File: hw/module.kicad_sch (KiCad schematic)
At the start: 42 parts, among them Q1 MUN 2211, U1 CFPS-39, U2 CFPS-39, U3 74LVC1G125, U4 74 LVC 1G3157GW,125, U5 MAX919, U6 STM32L010F4P6, U7 BAS70-7-F, U8 SS39ET

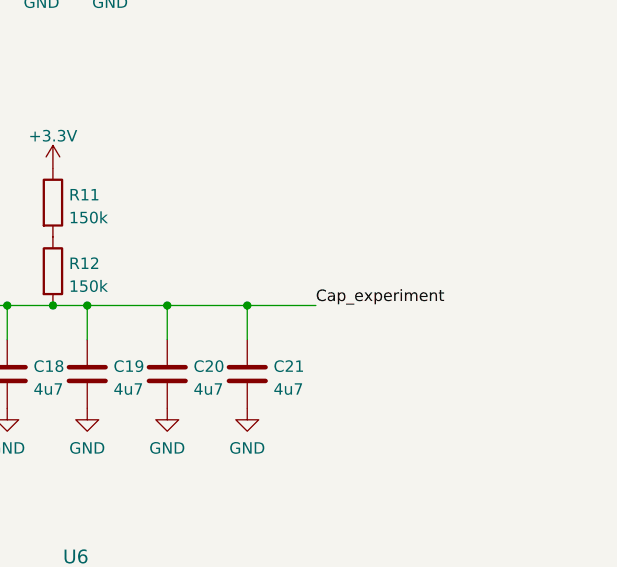
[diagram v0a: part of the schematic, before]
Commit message: Add extra resistor for capacitor measure, remove out-the-board wires
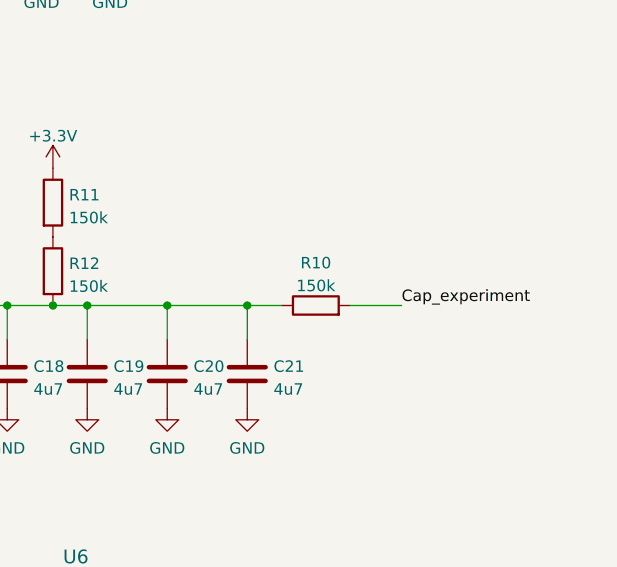
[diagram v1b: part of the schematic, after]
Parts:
- added R10: 150k, Resistor_SMD:R_0201_0603Metric_Pad0.64x0.40mm_HandSolder, symbol Device:R
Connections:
- net Cap_experiment: now also R10.2; no longer C16.1, C17.1, C18.1, C19.1, C20.1, C21.1, R12.2
- new net: C16.1, C17.1, C18.1, C19.1, C20.1, C21.1, R10.1, R12.2
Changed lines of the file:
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@@
   (junction (at 237.49 78.74) (diameter 0) (color 0 0 0 0)
   )
+  (junction (at 246.38 78.74) (diameter 0) (color 0 0 0 0)
+  )
   (junction (at 74.93 49.53) (diameter 0) (color 0 0 0 0)
   )
@@
   )
   (junction (at 228.6 78.74) (diameter 0) (color 0 0 0 0)
-  )
-  (junction (at 246.38 78.74) (diameter 0) (color 0 0 0 0)
   )
   (junction (at 231.14 33.02) (diameter 0) (color 0 0 0 0)
@@
     (stroke (width 0) (type default) (color 0 0 0 0))
   )
-  (wire (pts (xy 254 78.74) (xy 246.38 78.74))
-    (stroke (width 0) (type default) (color 0 0 0 0))
-  )
   (wire (pts (xy 257.81 138.43) (xy 281.94 138.43))
     (stroke (width 0) (type default) (color 0 0 0 0))
   )
+  (wire (pts (xy 257.81 78.74) (xy 263.525 78.74))
+    (stroke (width 0) (type default) (color 0 0 0 0))
+  )
   (wire (pts (xy 182.88 27.94) (xy 182.88 25.4))
     (stroke (width 0) (type default) (color 0 0 0 0))
@@
   )
   (wire (pts (xy 31.75 187.96) (xy 31.75 189.23))
+    (stroke (width 0) (type default) (color 0 0 0 0))
+  )
+  (wire (pts (xy 250.19 78.74) (xy 246.38 78.74))
     (stroke (width 0) (type default) (color 0 0 0 0))
   )
@@
     (effects (font (size 1.27 1.27)) (justify left bottom))
   )
-  (label "Cap_experiment" (at 254 78.74 0)
+  (label "Cap_experiment" (at 263.525 78.74 0)
     (effects (font (size 1.27 1.27)) (justify left bottom))
   )
@@
     )
     (pin "1")
+  )
+  (symbol (lib_id "Device:R") (at 254 78.74 90) (unit 1)
+    (in_bom yes) (on_board yes) (fields_autoplaced)
+    (property "Reference" "R10" (id 0) (at 254 74.0242 90))
+    (property "Value" "150k" (id 1) (at 254 76.5611 90))
+    (property "Footprint" "Resistor_SMD:R_0201_0603Metric_Pad0.64x0.40mm_HandSolder" (id 2) (at 254 80.518 90)
+      (effects (font (size 1.27 1.27)) hide)
+    )
+    (property "Datasheet" "~" (id 3) (at 254 78.74 0)
+      (effects (font (size 1.27 1.27)) hide)
+    )
+    (pin "1")
+    (pin "2")
   )
   (symbol (lib_id "power:GND") (at 31.75 189.23 0) (unit 1)
@@
       (reference "R9") (unit 1) (value "10k") (footprint "Resistor_SMD:R_0201_0603Metric_Pad0.64x0.40mm_HandSolder")
     )
+    (path "/1bc4374f-5e0f-4c16-9e5b-a3a33541057e"
+      (reference "R10") (unit 1) (value "150k") (footprint "Resistor_SMD:R_0201_0603Metric_Pad0.64x0.40mm_HandSolder")
+    )
     (path "/c3b088e6-8fb8-4f54-b8cc-ac4fee9ad1e4"

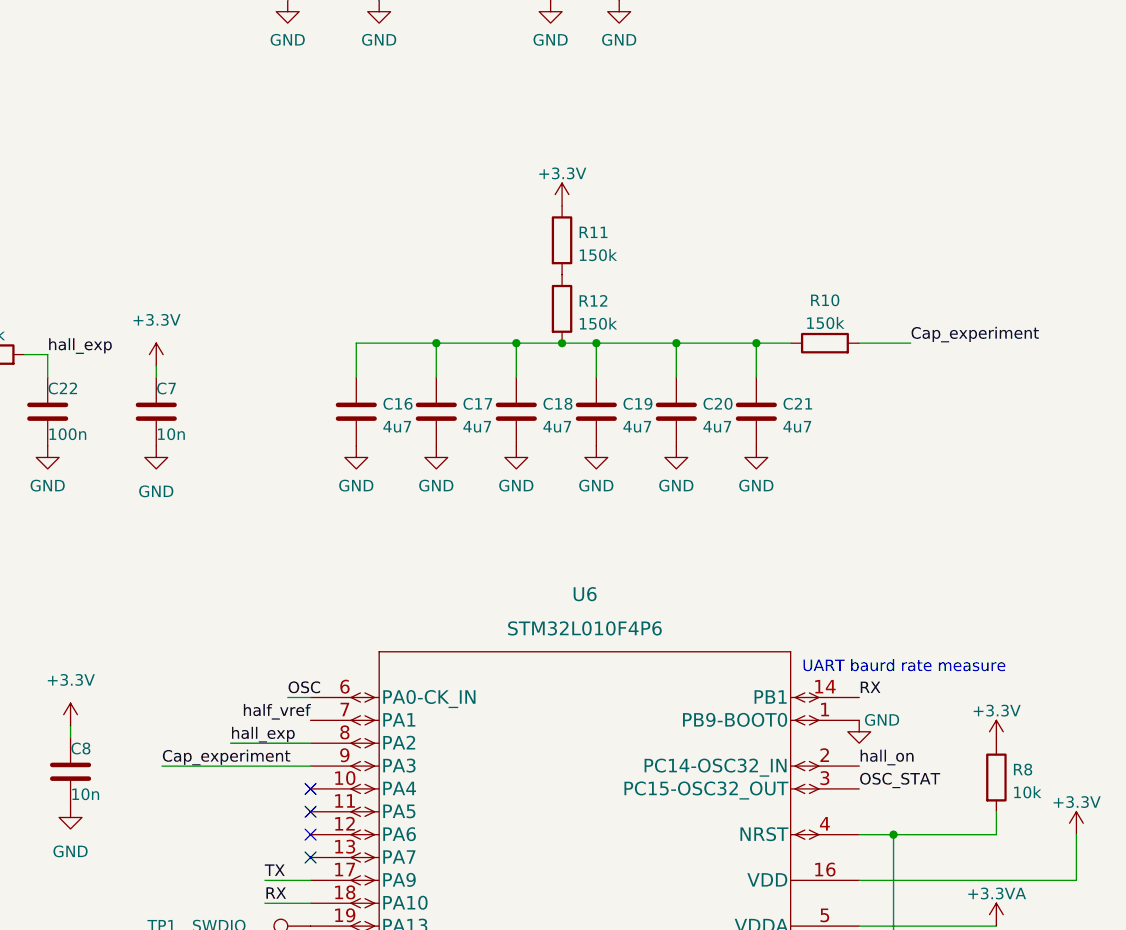
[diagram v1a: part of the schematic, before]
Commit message: 0603 passives
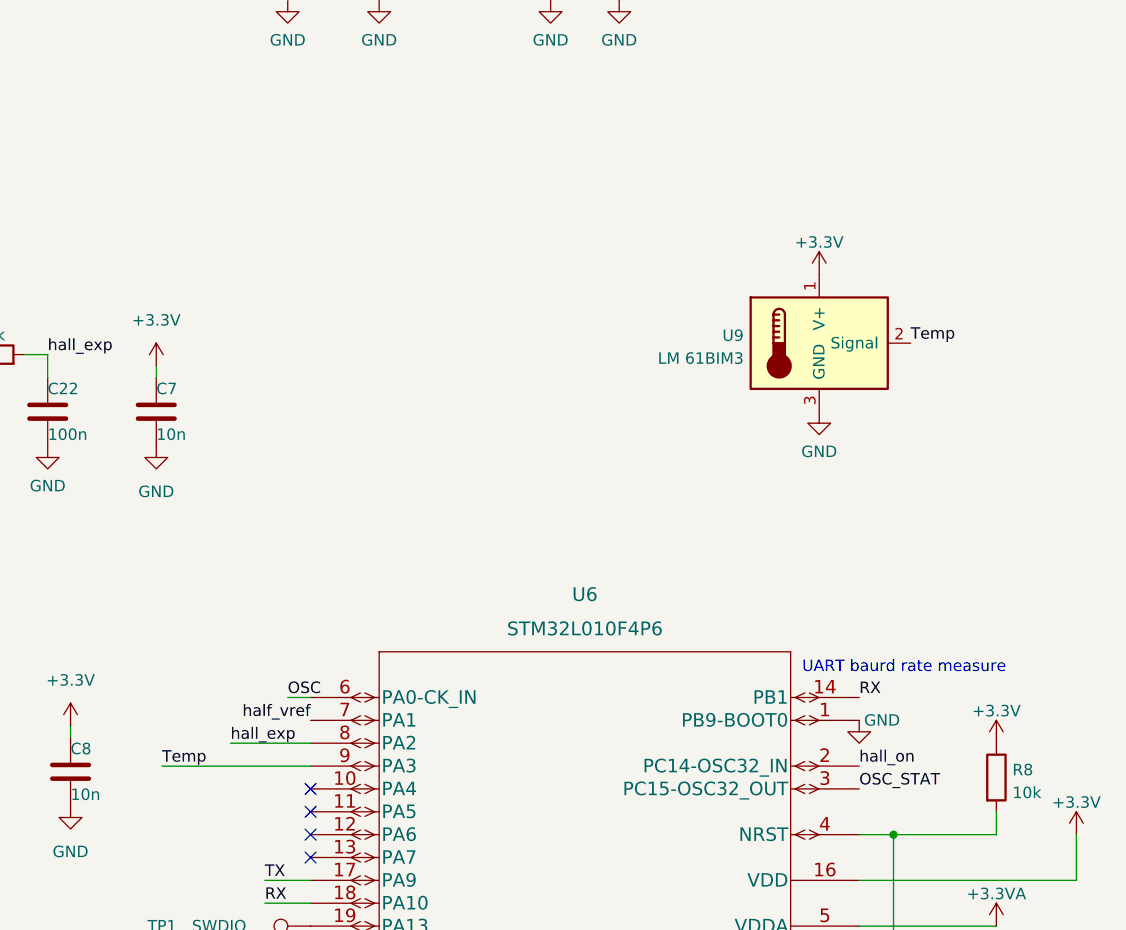
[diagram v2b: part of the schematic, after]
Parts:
- removed C16, C17, C18, C19, C20, C21: 4u7, Capacitor_SMD:C_0402_1005Metric_Pad0.74x0.62mm_HandSolder, symbol Device:C
- removed R10, R11, R12: 150k, Resistor_SMD:R_0201_0603Metric_Pad0.64x0.40mm_HandSolder, symbol Device:R
- added U9: LM 61BIM3, Package_TO_SOT_SMD:SOT-23_Handsoldering, symbol Sensor_Temperature:TSIC206-TO92
- C1, C11, C12, C13, C14, C15, C2, C22, C5, C6, C7, C8: footprint Capacitor_SMD:C_0201_0603Metric_Pad0.64x0.40mm_HandSolder -> Capacitor_SMD:C_0603_1608Metric_Pad1.08x0.95mm_HandSolder
- L1: footprint Inductor_SMD:L_0201_0603Metric_Pad0.64x0.40mm_HandSolder -> Inductor_SMD:L_0603_1608Metric_Pad1.05x0.95mm_HandSolder
- R1, R2, R3, R4, R5, R6, R7, R8, R9: footprint Resistor_SMD:R_0201_0603Metric_Pad0.64x0.40mm_HandSolder -> Resistor_SMD:R_0603_1608Metric_Pad0.98x0.95mm_HandSolder
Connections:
- net +3.3V: now also U9.1 (V+)
- net GND: now also U9.3 (GND)
- net Cap_experiment renamed Temp
- net Temp: now also U9.2 (Signal)

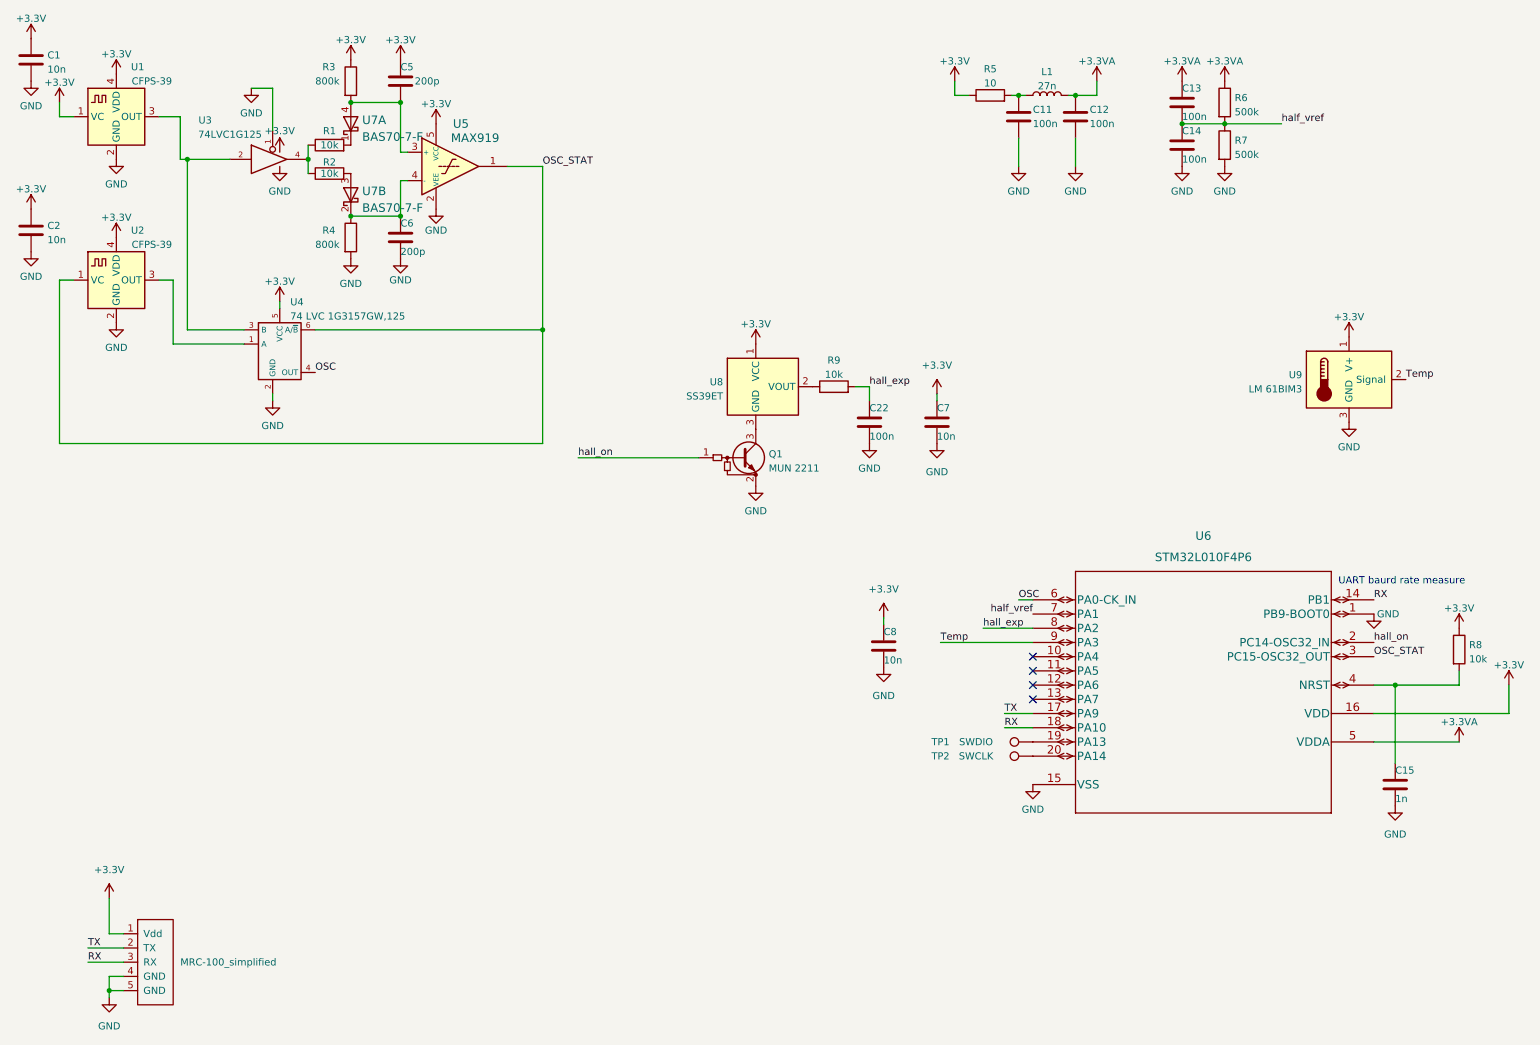
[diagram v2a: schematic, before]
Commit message: Redraw sch for the datasheet
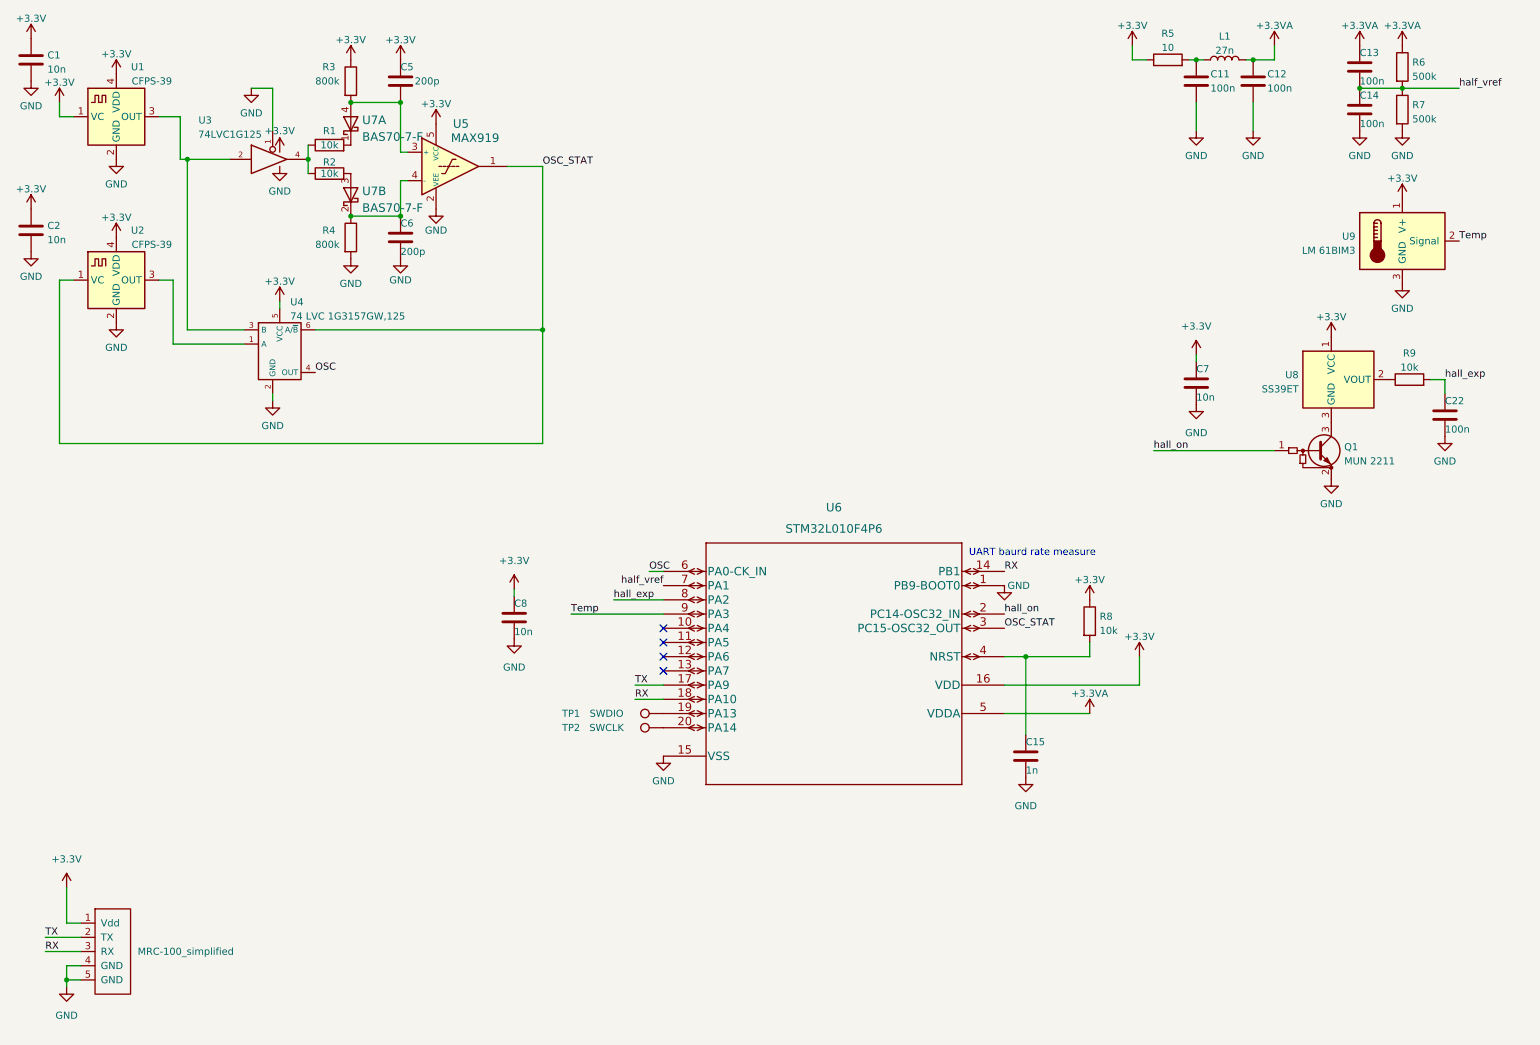
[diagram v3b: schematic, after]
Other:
- company: (none) -> SZTE Móra Ferenc Szakkollégium
- title: (none) -> MRC-100 SU modul
- moved on the sheet: C11, C12, C13, C14, C15, C22, C7, C8, L1, Q1, R5, R6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
